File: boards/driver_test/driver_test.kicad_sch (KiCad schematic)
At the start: 22 parts, among them J1 DIN41612_03x32_C, Q1 MMBT2222, Q2 MMBT2907, Q3 MMBT2222, U1 AD1582BRTZ

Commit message: Driver: some high-level board rearrangement and addition of 3d models
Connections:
- net GAR1: now also J1.c3; no longer J1.a1
- net GAR2: now also J1.c1; no longer J1.a3
- net GBR1: now also J1.c4; no longer J1.a2
- net GBR2: now also J1.c2; no longer J1.a4
- net RCD1: now also J1.c18; no longer J1.a18
- net RCD2: now also J1.c22; no longer J1.a22
- net RFD1: now also J1.c16; no longer J1.a16
- net RFD2: now also J1.c20; no longer J1.a20
- net RSTRN1: now also J1.c30; no longer J1.a30
- net SETRN1: now also J1.c32; no longer J1.a32
- net STR1: now also J1.c9; no longer J1.a9
- net STR2: now also J1.c10; no longer J1.a10
- net XCN1: now also J1.c19; no longer J1.a19
- net XCN2: now also J1.c23; no longer J1.a23
- net XFN1: now also J1.c17; no longer J1.a17
- net XFN2: now also J1.c21; no longer J1.a21
- net XRST1: now also J1.c29; no longer J1.a29
- net XSET1: now also J1.c31; no longer J1.a31
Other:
- sheet 40311 ports: added 4033nA, 4036nA; removed 0V, PWR
- sheet 40312 ports: added 4033nA, 4036nA; removed 0V, PWR
- sheet 40313 ports: added 4033nA, 4036nA; removed 0V, PWR
- sheet 40314 ports: added 4033nA, 4036nA; removed 0V, PWR
- sheet 40331 ports: added 4036nA, BPLIZ; removed 0V, PWR
- sheet 40601a ports: added BPLSWZ; removed PWR
- sheet 40601b ports: added BPLSWZ; removed PWR
- sheet Reset ports: added 4036nA, BPLIZ; removed 0V, PWR
- sheet Set ports: added 4036nA, BPLIZ; removed 0V, PWR

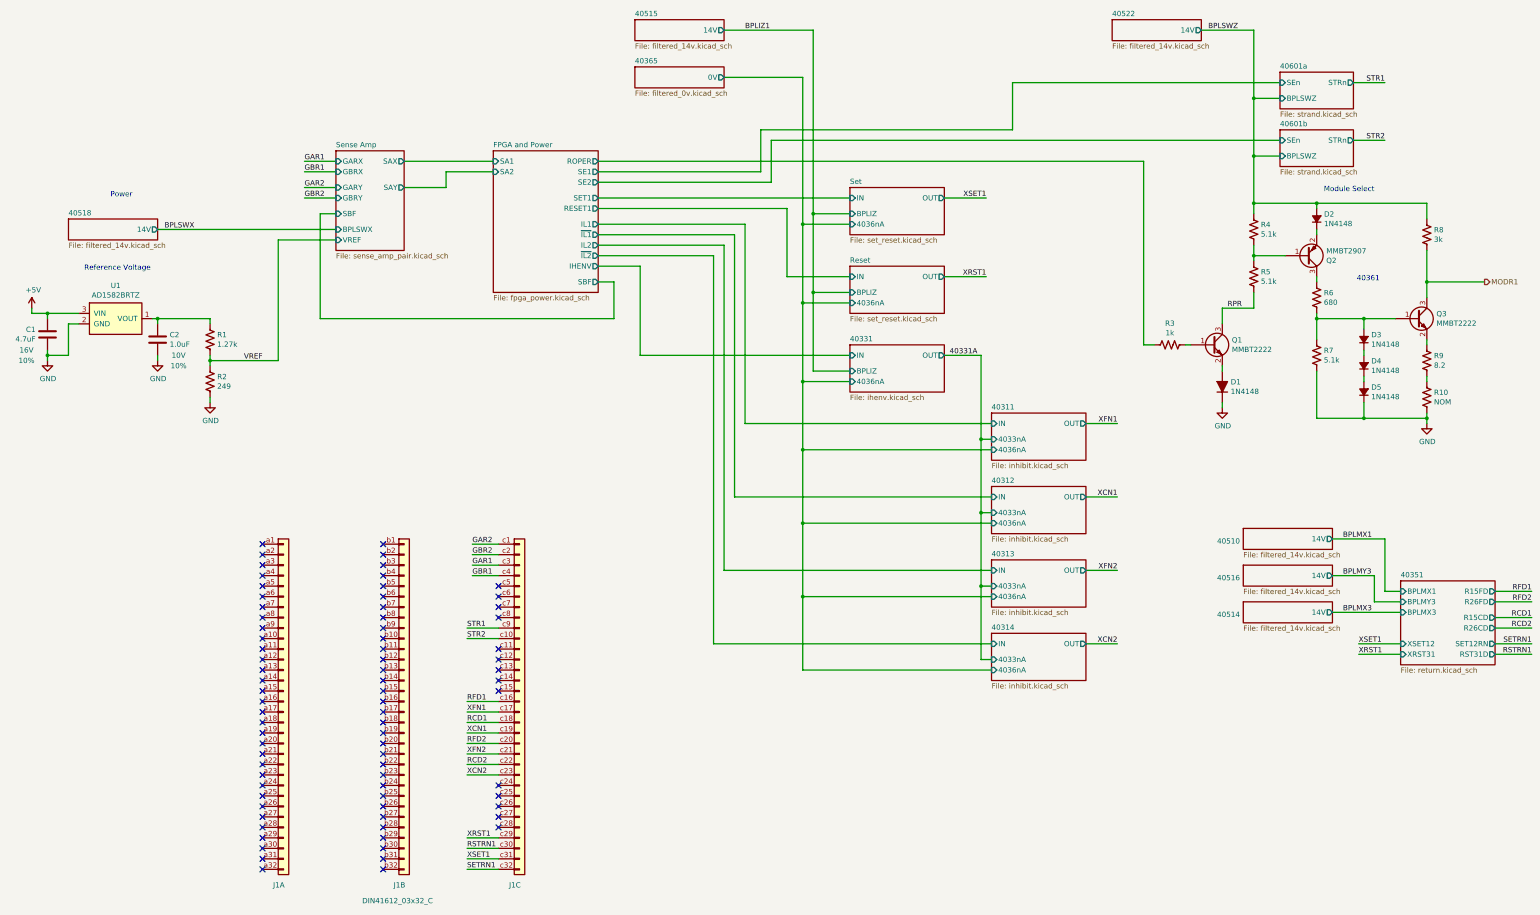
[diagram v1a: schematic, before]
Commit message: Driver test: completed much of the preliminary layout.
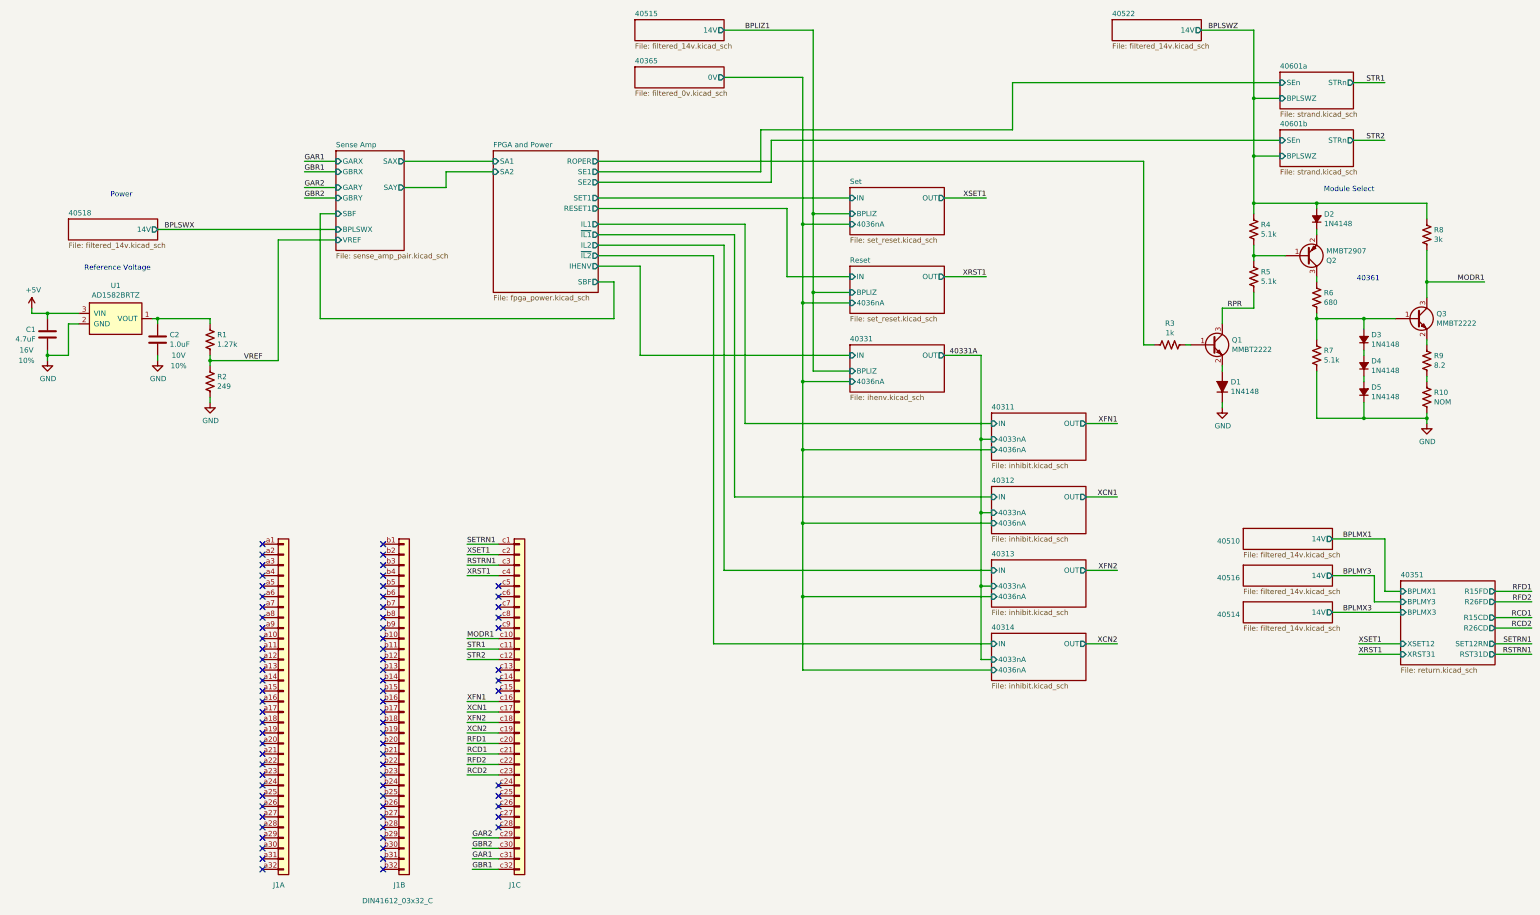
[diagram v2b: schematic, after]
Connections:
- net GAR1: now also J1.c31; no longer J1.c3
- net GAR2: now also J1.c29; no longer J1.c1
- net GBR1: now also J1.c32; no longer J1.c4
- net GBR2: now also J1.c30; no longer J1.c2
- net MODR1: now also J1.c10
- net RCD1: now also J1.c21; no longer J1.c18
- net RCD2: now also J1.c23; no longer J1.c22
- net RFD1: now also J1.c20; no longer J1.c16
- net RFD2: now also J1.c22; no longer J1.c20
- net RSTRN1: now also J1.c3; no longer J1.c30
- net SETRN1: now also J1.c1; no longer J1.c32
- net STR1: now also J1.c11; no longer J1.c9
- net STR2: now also J1.c12; no longer J1.c10
- net XCN1: now also J1.c17; no longer J1.c19
- net XCN2: now also J1.c19; no longer J1.c23
- net XFN1: now also J1.c16; no longer J1.c17
- net XFN2: now also J1.c18; no longer J1.c21
- net XRST1: now also J1.c4; no longer J1.c29
- net XSET1: now also J1.c2; no longer J1.c31
- no-connect marks 78 -> 77

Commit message: Driver test: finished up board layout
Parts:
- added H1, H2, H3, H4, H5, H6: MountingHole_Pad, lachesis:MountingHole_No2_Pad, symbol Mechanical:MountingHole_Pad
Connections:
- net GND: now also H1.1, H2.1, H3.1, H4.1, H5.1, H6.1

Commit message: Driver test: some updates to component values based on new documentation
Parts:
- C2: Rating 10V -> 25V
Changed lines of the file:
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@@
       (effects (font (size 1.27 1.27)) hide)
     )
-    (property "Rating" "10V" (id 7) (at 58.42 102.87 0))
+    (property "Rating" "25V" (id 7) (at 58.42 102.87 0))
     (property "Tolerance" "10%" (id 8) (at 58.42 105.41 0))
     (pin "1")
@@
     )
     (path "/c196771a-fa22-4343-a89f-be4540560780/00000000-0000-0000-0000-000061b55c06"
-      (reference "C8") (unit 1) (value "0.33uF") (footprint "Capacitor_SMD:C_0603_1608Metric")
+      (reference "C8") (unit 1) (value "100pF") (footprint "Capacitor_SMD:C_0603_1608Metric")
     )
     (path "/c196771a-fa22-4343-a89f-be4540560780/00000000-0000-0000-0000-000061ad1b2d"
@@
     )
     (path "/a15a860d-e886-4151-b20b-0f1fdf1eaddf/00000000-0000-0000-0000-0000635b04dd"
-      (reference "C12") (unit 1) (value "10nF") (footprint "Capacitor_SMD:C_0603_1608Metric")
+      (reference "C12") (unit 1) (value "0.01uF") (footprint "Capacitor_SMD:C_0603_1608Metric")
     )
     (path "/a15a860d-e886-4151-b20b-0f1fdf1eaddf/00000000-0000-0000-0000-00006359bb40"
@@
     )
     (path "/a15a860d-e886-4151-b20b-0f1fdf1eaddf/00000000-0000-0000-0000-0000635a5721"
-      (reference "C14") (unit 1) (value "0.1uF") (footprint "Capacitor_SMD:C_0603_1608Metric")
+      (reference "C14") (unit 1) (value "0.01uF") (footprint "Capacitor_SMD:C_0603_1608Metric")
     )
     (path "/a15a860d-e886-4151-b20b-0f1fdf1eaddf/00000000-0000-0000-0000-0000635a572b"
-      (reference "C15") (unit 1) (value "0.1uF") (footprint "Capacitor_SMD:C_0603_1608Metric")
+      (reference "C15") (unit 1) (value "0.01uF") (footprint "Capacitor_SMD:C_0603_1608Metric")
     )
     (path "/3cf15102-d63a-4525-b340-a08e48783995/00000000-0000-0000-0000-0000628400bf"
@@
     )
     (path "/a15a860d-e886-4151-b20b-0f1fdf1eaddf/00000000-0000-0000-0000-00006358f0d6"
-      (reference "R31") (unit 1) (value "470") (footprint "Resistor_SMD:R_0603_1608Metric")
+      (reference "R31") (unit 1) (value "100") (footprint "Resistor_SMD:R_0603_1608Metric")
     )
     (path "/a15a860d-e886-4151-b20b-0f1fdf1eaddf/00000000-0000-0000-0000-00006358f0dc"
-      (reference "R32") (unit 1) (value "470") (footprint "Resistor_SMD:R_0603_1608Metric")
+      (reference "R32") (unit 1) (value "100") (footprint "Resistor_SMD:R_0603_1608Metric")
     )
     (path "/a15a860d-e886-4151-b20b-0f1fdf1eaddf/00000000-0000-0000-0000-00006358f125"
-      (reference "R33") (unit 1) (value "470") (footprint "Resistor_SMD:R_0603_1608Metric")
+      (reference "R33") (unit 1) (value "100") (footprint "Resistor_SMD:R_0603_1608Metric")
     )
     (path "/a15a860d-e886-4151-b20b-0f1fdf1eaddf/00000000-0000-0000-0000-00006358f12b"
-      (reference "R34") (unit 1) (value "470") (footprint "Resistor_SMD:R_0603_1608Metric")
+      (reference "R34") (unit 1) (value "100") (footprint "Resistor_SMD:R_0603_1608Metric")
     )
     (path "/e9ae5b56-9661-4785-af7a-48e9ad409f89/00000000-0000-0000-0000-0000623343fa"

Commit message: Driver test: updated schematic with new coarse tuning resistance values for all 3 current driver types
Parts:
- R10: value NOM -> 1.5 NOM
- R9: value 8.2 -> 10
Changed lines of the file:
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@@
       (effects (font (size 1.27 1.27)) (justify left))
     )
-    (property "Value" "8.2" (id 1) (at 362.4072 105.283 0)
+    (property "Value" "10" (id 1) (at 362.4072 105.283 0)
       (effects (font (size 1.27 1.27)) (justify left))
     )
@@
       (effects (font (size 1.27 1.27)) (justify left))
     )
-    (property "Value" "NOM" (id 1) (at 362.4072 114.173 0)
+    (property "Value" "1.5 NOM" (id 1) (at 362.4072 114.173 0)
       (effects (font (size 1.27 1.27)) (justify left))
     )
@@
     )
     (path "/3165d2e9-2acb-4a76-a863-fd9dbfda5d16"
-      (reference "R9") (unit 1) (value "8.2") (footprint "Resistor_SMD:R_0603_1608Metric")
+      (reference "R9") (unit 1) (value "10") (footprint "Resistor_SMD:R_0603_1608Metric")
     )
     (path "/a3bda3bf-1a44-4698-bb7f-9e55ca267c99"
-      (reference "R10") (unit 1) (value "NOM") (footprint "Resistor_SMD:R_0603_1608Metric")
+      (reference "R10") (unit 1) (value "1.5 NOM") (footprint "Resistor_SMD:R_0603_1608Metric")
     )
     (path "/c196771a-fa22-4343-a89f-be4540560780/35dfe0d1-7c61-4f1c-8456-3f0475c0a93a"
@@
     )
     (path "/e9ae5b56-9661-4785-af7a-48e9ad409f89/00000000-0000-0000-0000-00006235467b"
-      (reference "R42") (unit 1) (value "7.5") (footprint "Resistor_SMD:R_0805_2012Metric")
+      (reference "R42") (unit 1) (value "9.1") (footprint "Resistor_SMD:R_0805_2012Metric")
     )
     (path "/e9ae5b56-9661-4785-af7a-48e9ad409f89/00000000-0000-0000-0000-000062968639"
@@
     )
     (path "/3c199913-5469-4947-ae17-e3b4a93e50a4/00000000-0000-0000-0000-00006235467b"
-      (reference "R51") (unit 1) (value "7.5") (footprint "Resistor_SMD:R_0805_2012Metric")
+      (reference "R51") (unit 1) (value "9.1") (footprint "Resistor_SMD:R_0805_2012Metric")
     )
     (path "/3c199913-5469-4947-ae17-e3b4a93e50a4/00000000-0000-0000-0000-000062968639"
@@
     )
     (path "/b442958e-7c6c-4170-9085-089ed11b4c6e/00000000-0000-0000-0000-000062448410"
-      (reference "R55") (unit 1) (value "3.9") (footprint "Resistor_SMD:R_0603_1608Metric")
+      (reference "R55") (unit 1) (value "4.7") (footprint "Resistor_SMD:R_0603_1608Metric")
     )
     (path "/b442958e-7c6c-4170-9085-089ed11b4c6e/00000000-0000-0000-0000-000062958d7b"
@@
     )
     (path "/2c7de5be-e684-4b15-8fa0-a21070b723e4/00000000-0000-0000-0000-000062448410"
-      (reference "R65") (unit 1) (value "3.9") (footprint "Resistor_SMD:R_0603_1608Metric")
+      (reference "R65") (unit 1) (value "4.7") (footprint "Resistor_SMD:R_0603_1608Metric")
     )
     (path "/2c7de5be-e684-4b15-8fa0-a21070b723e4/00000000-0000-0000-0000-000062958d7b"
@@
     )
     (path "/f424afed-3e5b-4582-850d-0a724d0d4705/00000000-0000-0000-0000-000062448410"
-      (reference "R69") (unit 1) (value "3.9") (footprint "Resistor_SMD:R_0603_1608Metric")
+      (reference "R69") (unit 1) (value "4.7") (footprint "Resistor_SMD:R_0603_1608Metric")
     )
     (path "/f424afed-3e5b-4582-850d-0a724d0d4705/00000000-0000-0000-0000-000062958d7b"
@@
     )
     (path "/1bcddc41-f45d-4815-9d74-0ae4c475a25f/00000000-0000-0000-0000-000062448410"
-      (reference "R73") (unit 1) (value "3.9") (footprint "Resistor_SMD:R_0603_1608Metric")
+      (reference "R73") (unit 1) (value "4.7") (footprint "Resistor_SMD:R_0603_1608Metric")
     )
     (path "/1bcddc41-f45d-4815-9d74-0ae4c475a25f/00000000-0000-0000-0000-000062958d7b"
